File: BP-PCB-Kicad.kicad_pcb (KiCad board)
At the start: 4 copper layers, 120.7 x 98 mm, 74 parts, among them IC1 LMT84DCKT, J1 A3C-50DA-2DSA_71_, J13 Conn_01x20, J14 Conn_01x20, J15 DF14-30P-1.25H_35_, J16 A3C-50DA-2DSA_71_, J17 A3C-4DA-2DSA_71_, J18 A3C-4DA-2DSA_71_, J19 Molex 55460-0272, J2 A3C-50DA-2DSA_71_, J21 Molex 55460-0272, J22 Molex 55460-0272, J23 DF14-15P-1.25H52, J3 A3C-4DA-2DSA_71_, J4 A3C-4DA-2DSA_71_, J5 A3C-50DA-2DSA_71_, J6 A3C-50DA-2DSA_71_, J7 DF14-15P-1.25H52, J8 DF14-15P-1.25H52, Q1 SSM6K514NU,LF, Q2 SSM6K514NU,LF, Q3 SSM6K514NU,LF, Q4 SSM6K514NU,LF, Q5 SSM6K514NU,LF, Q6 SSM6K514NU,LF, U1 LTC4361CTS8-2TRMPBF, U2 LTC4361CTS8-2TRMPBF, U3 SN74CB3Q3257DBQR, U5 SN74CB3Q3257DBQR, U6 LTC4389IMS-4#PBF, U7 LTC4389IMS-4#PBF

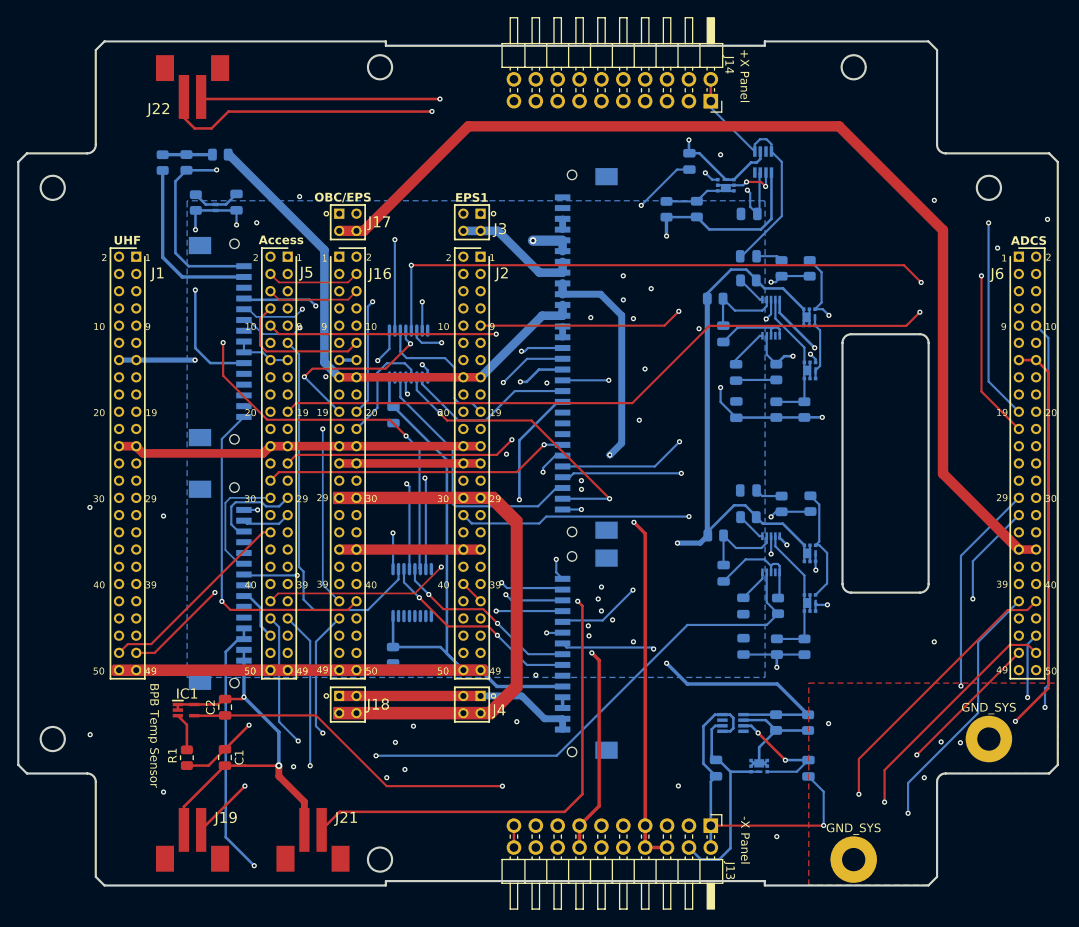
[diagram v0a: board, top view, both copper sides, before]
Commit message: Finished routing and NO DRC errors
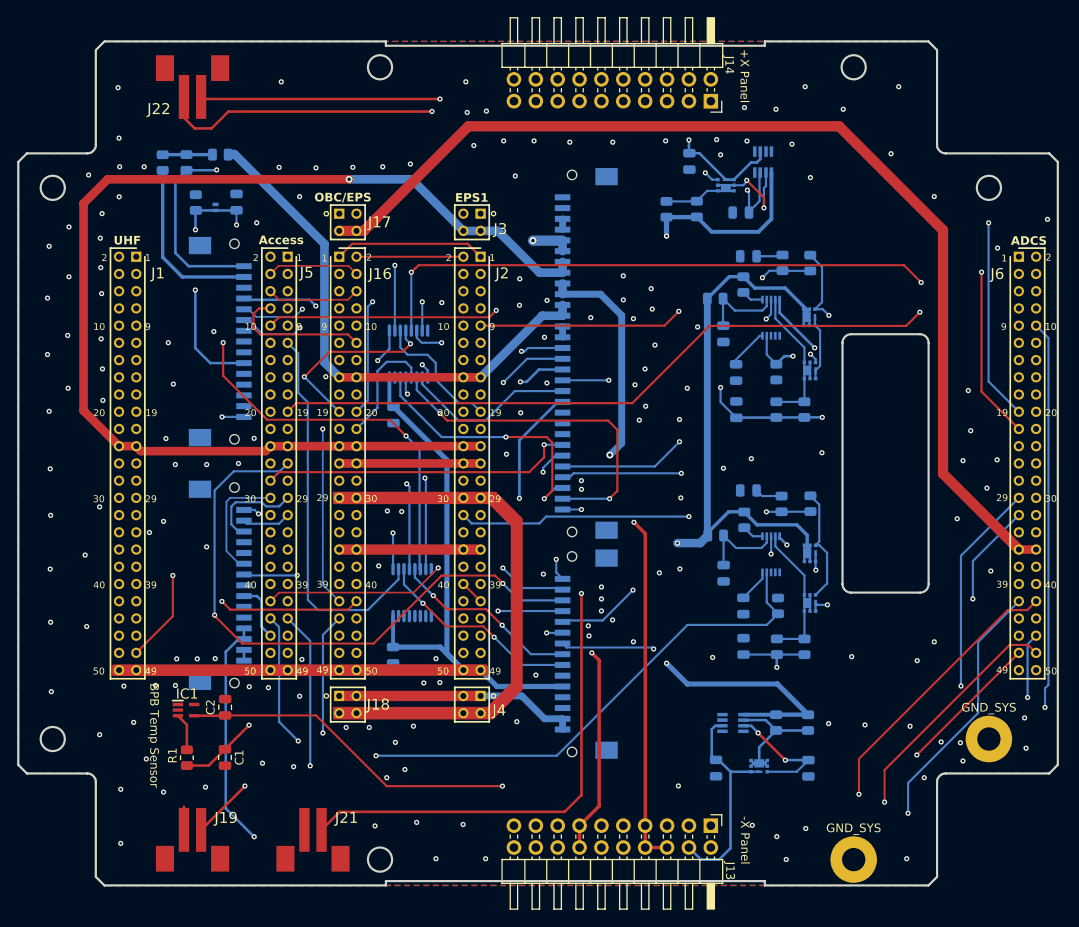
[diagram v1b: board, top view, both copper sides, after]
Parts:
- moved C4 0.98 mm to (114.6, 45.7)
- moved R5 0.75 mm to (114.9, 54.0), turned to -90 degrees
- moved R7 0.65 mm to (119.5, 51.5)
- moved R8 0.62 mm to (122.7, 51.5)
- moved R12 0.57 mm to (115.0, 81.3), turned to -90 degrees
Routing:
- net GND_SYS: track 271.3 -> 6.93 mm, vias 6 -> 130
- net SUP_UNREG_1: track 57.5 -> 134.9 mm, vias 0 -> 1
- net Thruster_1: track 52.3 -> 70.6 mm
- net ANALOG_RSSI (UHF_to_RelayPIC): track 23.4 -> 30.6 mm, vias 0 -> 1
- net MUX-CCB_UART (MainPIC_to_FPGA): track 34.5 -> 40.5 mm
- net  V_IN (Unreg2 OCP to S-band RX): track 136.6 -> 131.9 mm
- net Net-(Q2-D_1): track 16.4 -> 20.8 mm
- net SPI_CS (ADCS_to_FM2): track 185.6 -> 181.7 mm
- net ANALOG_TEMP (UHF_to_RelayPIC): track 20.9 -> 24.5 mm
- net DIO_HW_Reset: track 66.5 -> 69.6 mm
- net SUP_3V3_1: track 179.7 -> 181.9 mm
- net MUX-ADCS UART (MainPIC_to_ADCS): track 85.0 -> 82.8 mm
- net OBC-SBAND_TX_UART_HK (Sband_TX_to_ComPic): track 38.9 -> 40.4 mm, vias 1 -> 2
- net DEP_SW12: track 68.7 -> 70.2 mm
- net Net-(U6-DRN): track 3.94 -> 2.56 mm
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
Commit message: Final routing v2
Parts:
- removed R18: 5 Ohm, Resistor_SMD:R_0805_2012Metric
- removed U7: LTC4389IMS-4#PBF, Custom-Footprints:LTC4380IMS-4#PBF
- added U4: LTC4380IMS-4#PBF, Custom-Footprints:LTC4380IMS-4#PBF, B.Cu at (118.1, 57.9)
- R16, R17: value 25m Ohm -> 25m
- R2: value 5 Ohm -> 2.5 Ohm
- U6: value LTC4389IMS-4#PBF -> LTC4380IMS-4#PBF
- moved U6 27.5 mm to (118.1, 85.4)
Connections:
- C13 pad 1: Net-(U7-VCC) -> Net-(U6-VCC)
- C14 pad 1: Net-(U7-TMR) -> Net-(U6-TMR)
- C8 pad 1: Net-(U6-VCC) -> Net-(U4-VCC)
- C9 pad 1: Net-(U6-TMR) -> Net-(U4-TMR)
- R11 pad 2: Net-(U7-VCC) -> Net-(U6-VCC)
- R12 pad 2: Net-(U7-DRN) -> Net-(U6-DRN)
- R14 pad 1: Net-(U7-GATE) -> Net-(U6-GATE)
- R15 pad 1: Net-(U7-GATE) -> Net-(U6-GATE)
- R4 pad 2: Net-(U6-VCC) -> Net-(U4-VCC)
- R5 pad 2: Net-(U6-DRN) -> Net-(U4-DRN)
- R7 pad 1: Net-(U6-GATE) -> Net-(U4-GATE)
- R8 pad 1: Net-(U6-GATE) -> Net-(U4-GATE)
- U6 pad 4: Net-(Q3-D_1) -> Net-(Q5-D_1)
- U6 pad 5:  V_IN (Unreg2 OCP to S-band TX) ->  V_IN (Unreg2 OCP to S-band RX)
- U6 pad 9: DIO_S-Band_TX_ON/OFF -> DIO_S-Band_RX_ON/OFF
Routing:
- net Net-(U4-GATE): track 0.00 -> 13.4 mm, vias 0 -> 2
- net Net-(U7-GATE): track 12.3 -> 0.00 mm, vias 2 -> 0
- net Net-(U7-VCC): track 10.1 -> 0.00 mm
- net Net-(U4-VCC): track 0.00 -> 9.76 mm
- net Net-(U4-TMR): track 0.00 -> 4.98 mm
- net Net-(U7-TMR): track 3.87 -> 0.00 mm
- net Net-(U4-DRN): track 0.00 -> 2.56 mm
- net Net-(U7-DRN): track 2.52 -> 0.00 mm
- net Net-(U6-TMR): track 4.98 -> 3.87 mm
- net Net-(U6-GATE): track 13.4 -> 12.3 mm

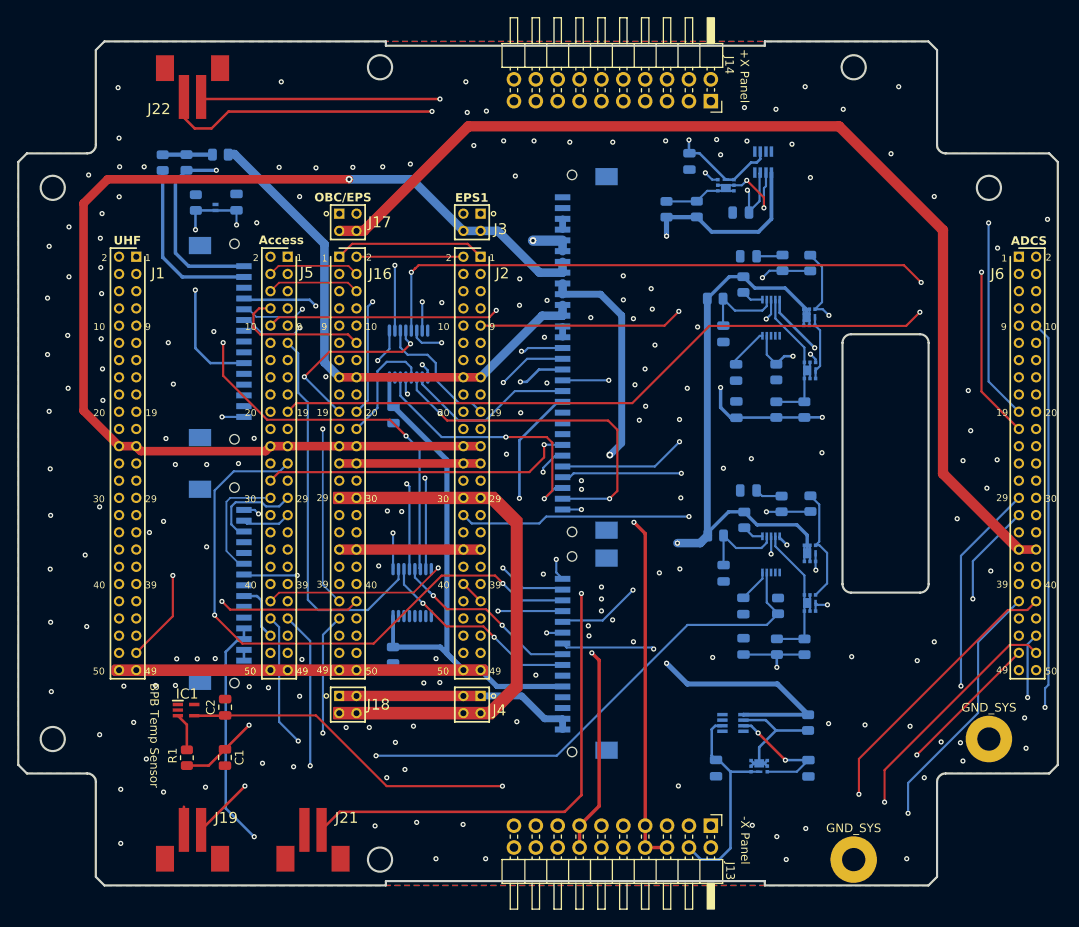
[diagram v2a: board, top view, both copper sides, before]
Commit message: Corrected OCP values in schematic and fixed PCB layout
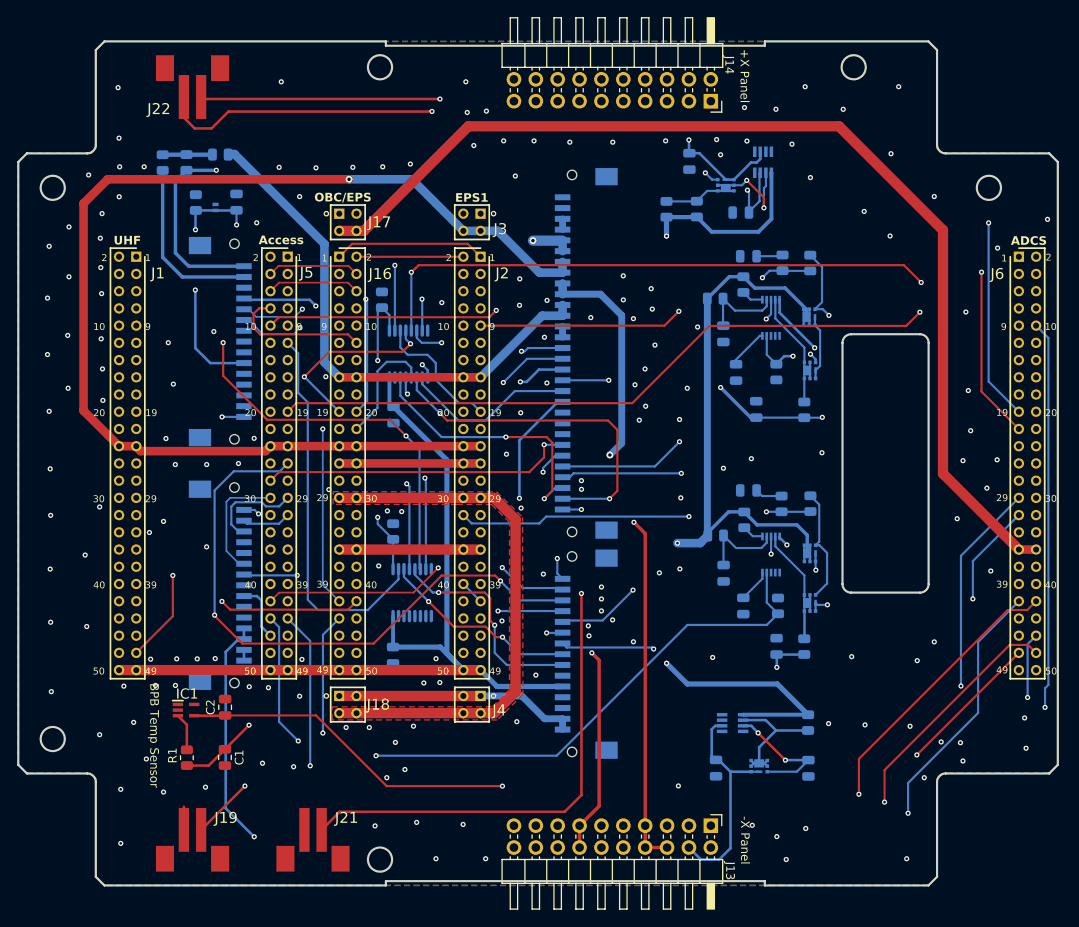
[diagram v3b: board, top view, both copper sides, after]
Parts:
- removed GND_SYS (x2): MountingHole_2.7mm_Pad, MountingHole:MountingHole_2.7mm_Pad
- R10, R17: value 25m -> 100k
- U4, U6: value LTC4380IMS-4#PBF -> LTC4380IMS-2#PBF; footprint Custom-Footprints:LTC4380IMS-4#PBF -> Custom-Footprints:LTC4380IMS-2#PBF
- moved R17 63.5 mm to (73.0, 55.8)
- moved R10 49.8 mm to (74.2, 82.7)
- moved C16 3.84 mm to (118.8, 96.0)
- moved R9 3.25 mm to (122.0, 68.6)
- moved R16 3.17 mm to (122.0, 96.1)
- moved C12 2.31 mm to (116.4, 68.5)
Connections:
- net MainPIC-MUX-ThermalPIC_UART renamed MUX-TCB_UART (MainPIC_to_ThermalPIC)
- net ThermalPIC-MUX-MainPIC_UART  renamed MUX-TCB_UART (ThermalPIC_to_MainPIC)
- J23 pad 7: MUX-Thruster UART_1 (MainPIC_to_Thruster) -> MUX-Thruster UART_1 (Thruster_to_MainPIC)
- J23 pad 8: MUX-Thruster UART_1 (Thruster_to_MainPIC) -> MUX-Thruster UART_1 (MainPIC_to_Thruster)
- R10 pad 1: Net-(Q3-D_1) -> GND_SYS
- R10 pad 2:  V_IN (Unreg2 OCP to S-band TX) -> DIO_MUX_SEL
- R17 pad 1: Net-(Q5-D_1) -> GND_SYS
- R17 pad 2:  V_IN (Unreg2 OCP to S-band RX) -> DIO_MUX_SEL
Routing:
- net RAW_POWER: track 0.00 -> 63.0 mm
- net SUP_3V3_1: track 181.8 -> 221.7 mm
- net DIO_MUX_SEL: track 44.3 -> 49.6 mm
- net  V_IN (Unreg2 OCP to S-band RX): track 131.9 -> 127.9 mm
- net MUX-Thruster UART_1 (Thruster_to_MainPIC): track 21.8 -> 25.6 mm
- net Net-(Q3-D_1): track 19.0 -> 15.7 mm
- net Net-(Q5-D_1): track 18.9 -> 15.7 mm
- net  V_IN (Unreg2 OCP to S-band TX): track 139.4 -> 137.6 mm
- net OBC-MUX_UART (ADCSPIC/EPS1PIC_to_MainPIC): track 22.6 -> 23.9 mm
- net MUX-Thruster UART_1 (MainPIC_to_Thruster): track 24.1 -> 23.0 mm
- net (no net): vias 0 -> 7
- added copper zone on F.Cu, net RAW_POWER

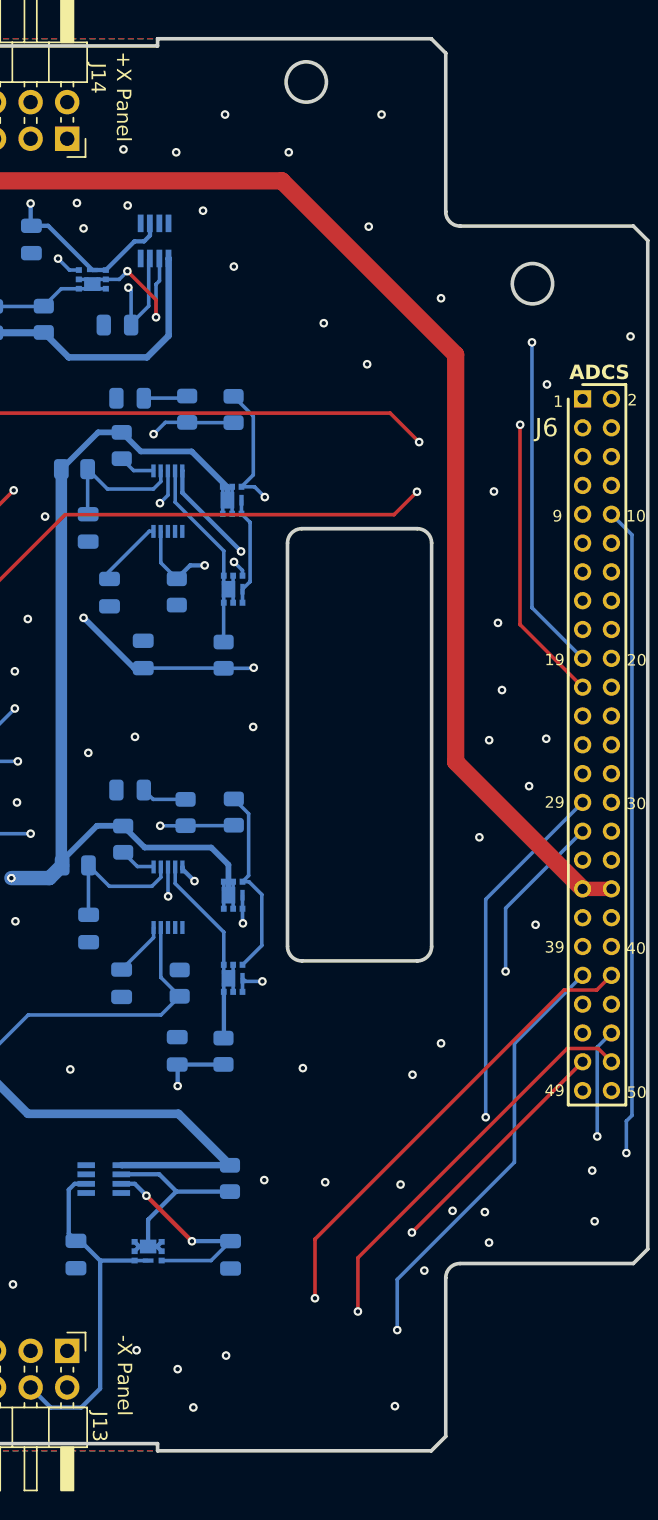
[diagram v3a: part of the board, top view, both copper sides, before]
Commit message: Added grounded mounting holes to schematics
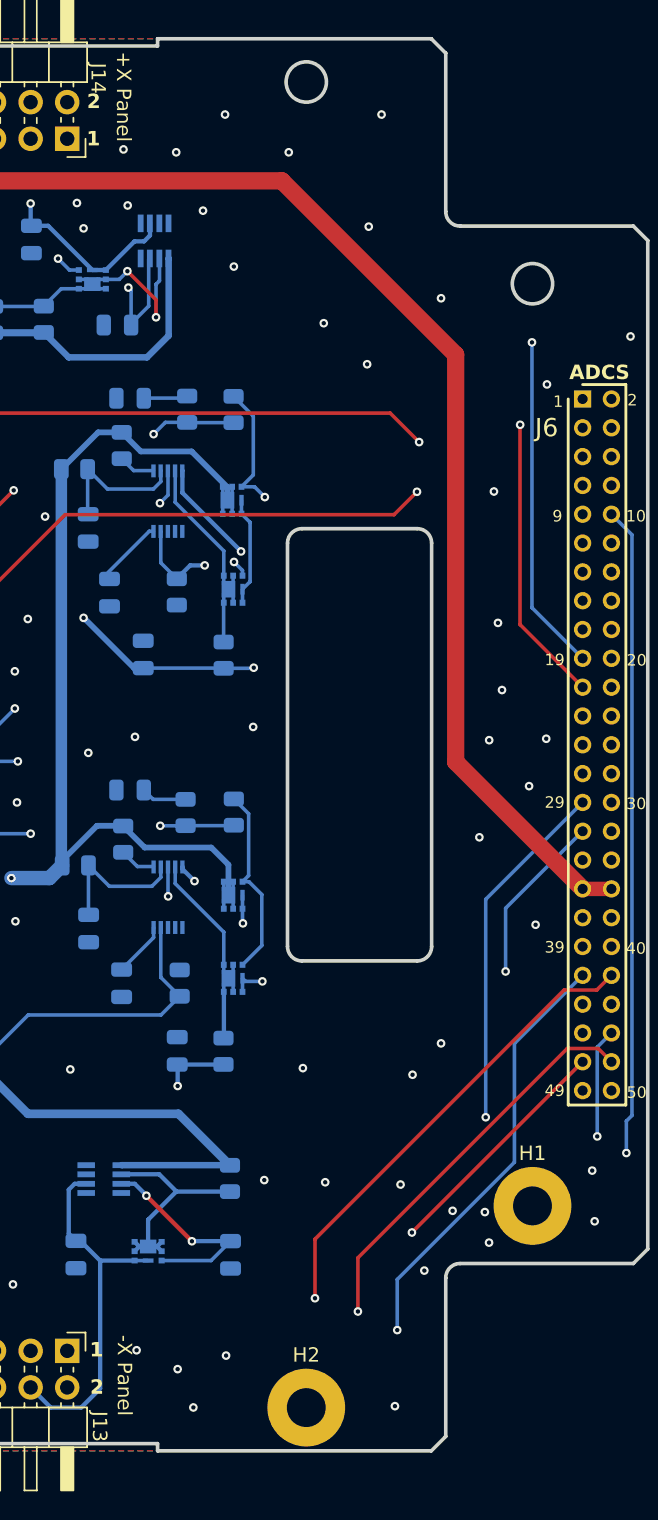
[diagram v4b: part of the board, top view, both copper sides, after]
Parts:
- added H1: MountingHole_Pad, MountingHole:MountingHole_2.7mm_Pad, F.Cu at (143.4, 106.8)
- added H2: MountingHole_Pad, MountingHole:MountingHole_2.7mm_Pad, F.Cu at (127.7, 120.8)
- IC1: value LMT84DCKT -> LMT84DCKT_LMT84DCKT
- U4, U6: value LTC4380IMS-2#PBF -> MS_10_ADI
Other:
- board text added: "1"
- board text added: "2"
- board text added: "TURAN-1 Backplane BBM Abbos Akramov"
- board text removed: "TURAN-1 Backplane BBM Akramov Abbos"

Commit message: Polished some power lines
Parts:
- moved R14 0.77 mm to (119.3, 78.7)
- moved R15 0.69 mm to (122.7, 78.8)
- moved C15 0.48 mm to (115.1, 77.7)
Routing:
- net SUP_UNREG_3: track 122.9 -> 126.0 mm
- net Net-(Q5-G): track 13.5 -> 15.1 mm
- net SUP_UNREG_2: track 110.7 -> 111.5 mm
- net Net-(U6-GATE): track 12.3 -> 13.1 mm
- net MCLR_ADCS_PIC: track 102.3 -> 101.6 mm
- net GND_SYS: vias 130 -> 142

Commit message: BBM version requested for fabrication
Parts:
- U1, U2: value LTC4361CTS8-2TRMPBF -> LTC4361-2
- moved R3 4.78 mm to (109.1, 48.9), turned to -90 degrees
- moved R20 1.31 mm to (109.1, 44.0)
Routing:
- net Net-(Q2-D_1): track 20.7 -> 32.5 mm
- net SUP_3V3_1: track 221.7 -> 222.5 mm
- net GND_SYS: vias 142 -> 139
- net (no net): vias 7 -> 5
